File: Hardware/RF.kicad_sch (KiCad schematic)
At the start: 5 parts, among them J2 Conn_Coaxial

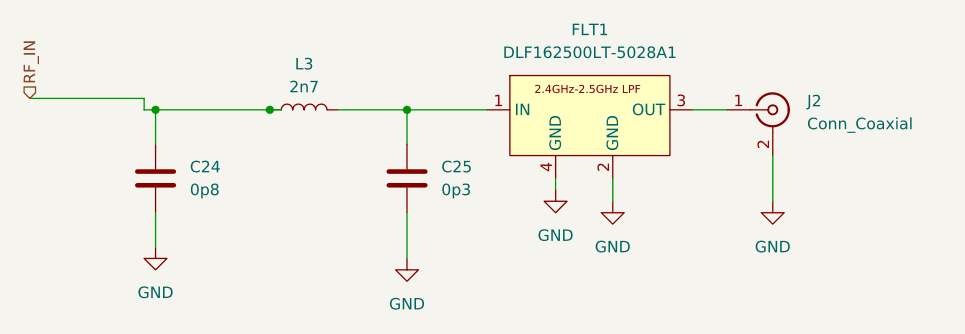
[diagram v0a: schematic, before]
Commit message: [EXECUTION ERC] : Le check électrique a bien marché sauf une erreur persistante sur VLXSMPS ce qui est un défaut du symbole créé et non du montage de découplage proposé par ST Microelectronics
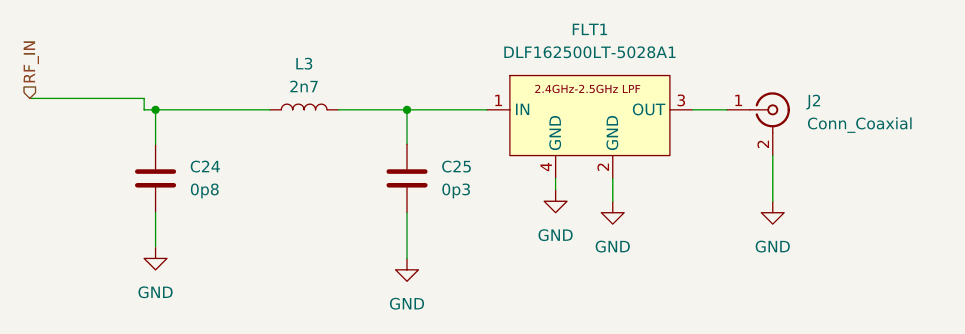
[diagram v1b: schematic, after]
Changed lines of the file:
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@@
 	(paper "A4")
 	(junction
-		(at 107.95 68.58)
+		(at 123.19 68.58)
 		(diameter 0)
 		(color 0 0 0 0)
@@
 		(color 0 0 0 0)
 	)
-	(junction
-		(at 123.19 68.58)
-		(diameter 0)
-		(color 0 0 0 0)
+	(wire
+		(pts
+			(xy 95.25 68.58) (xy 107.95 68.58)
+		)
+		(stroke
+			(width 0)
+			(type default)
+		)
 	)
 	(wire
@@
 	(wire
 		(pts
-			(xy 107.95 68.58) (xy 109.22 68.58)
-		)
-		(stroke
-			(width 0)
-			(type default)
-		)
-	)
-	(wire
-		(pts
 			(xy 115.57 68.58) (xy 123.19 68.58)
 		)
@@
 		(pts
 			(xy 146.05 76.2) (xy 146.05 78.74)
-		)
-		(stroke
-			(width 0)
-			(type default)
-		)
-	)
-	(wire
-		(pts
-			(xy 95.25 68.58) (xy 107.95 68.58)
 		)
 		(stroke
@@
 		(dnp no)
 		(fields_autoplaced yes)
-		(property "Reference" "#PWR?"
+		(property "Reference" "#PWR023"
 			(at 95.25 90.17 0)
 			(effects
@@
 			(project "Hardware"
 				(path "/ba4846b8-7c71-441f-b11b-b34cbea60d05/f30678ac-07b1-44be-9fb4-b413baff1170"
-					(reference "#PWR?")
+					(reference "#PWR023")
 					(unit 1)
 				)
@@
 		(dnp no)
 		(fields_autoplaced yes)
-		(property "Reference" "#PWR?"
+		(property "Reference" "#PWR020"
 			(at 139.7 83.82 0)
 			(effects
@@
 			(project "Hardware"
 				(path "/ba4846b8-7c71-441f-b11b-b34cbea60d05/f30678ac-07b1-44be-9fb4-b413baff1170"
-					(reference "#PWR?")
+					(reference "#PWR020")
 					(unit 1)
 				)
@@
 		(dnp no)
 		(fields_autoplaced yes)
-		(property "Reference" "#PWR?"
+		(property "Reference" "#PWR024"
 			(at 123.19 91.44 0)
 			(effects
@@
 			(project "Hardware"
 				(path "/ba4846b8-7c71-441f-b11b-b34cbea60d05/f30678ac-07b1-44be-9fb4-b413baff1170"
-					(reference "#PWR?")
+					(reference "#PWR024")
 					(unit 1)
 				)
@@
 		(dnp no)
 		(fields_autoplaced yes)
-		(property "Reference" "#PWR?"
+		(property "Reference" "#PWR022"
 			(at 163.83 85.09 0)
 			(effects
@@
 			(project "Hardware"
 				(path "/ba4846b8-7c71-441f-b11b-b34cbea60d05/f30678ac-07b1-44be-9fb4-b413baff1170"
-					(reference "#PWR?")
+					(reference "#PWR022")
 					(unit 1)
 				)
@@
 		(dnp no)
 		(fields_autoplaced yes)
-		(property "Reference" "#PWR?"
+		(property "Reference" "#PWR021"
 			(at 146.05 85.09 0)
 			(effects
@@
 			(project "Hardware"
 				(path "/ba4846b8-7c71-441f-b11b-b34cbea60d05/f30678ac-07b1-44be-9fb4-b413baff1170"
-					(reference "#PWR?")
-					(unit 1)
-				)
+					(reference "#PWR021")
+					(unit 1)
+				)

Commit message: [FOOTPRINT ASSIGNMENT] : Ajout des footprints à chaque élément
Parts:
- C24, C25: footprint (none) -> Capacitor_SMD:C_0402_1005Metric
- J2: footprint (none) -> Connector_Coaxial:U.FL_Hirose_U.FL-R-SMT-1_Vertical
- L3: footprint (none) -> Inductor_SMD:L_0402_1005Metric
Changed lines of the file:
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@@
 			)
 		)
-		(property "Footprint" ""
+		(property "Footprint" "Inductor_SMD:L_0402_1005Metric"
 			(at 111.76 68.58 0)
 			(effects
@@
 			)
 		)
-		(property "Footprint" ""
+		(property "Footprint" "Capacitor_SMD:C_0402_1005Metric"
 			(at 124.1552 80.01 0)
 			(effects
@@
 			)
 		)
-		(property "Footprint" ""
+		(property "Footprint" "Capacitor_SMD:C_0402_1005Metric"
 			(at 96.2152 80.01 0)
 			(effects
@@
 			)
 		)
-		(property "Footprint" ""
+		(property "Footprint" "Connector_Coaxial:U.FL_Hirose_U.FL-R-SMT-1_Vertical"
 			(at 163.83 68.58 0)
 			(effects

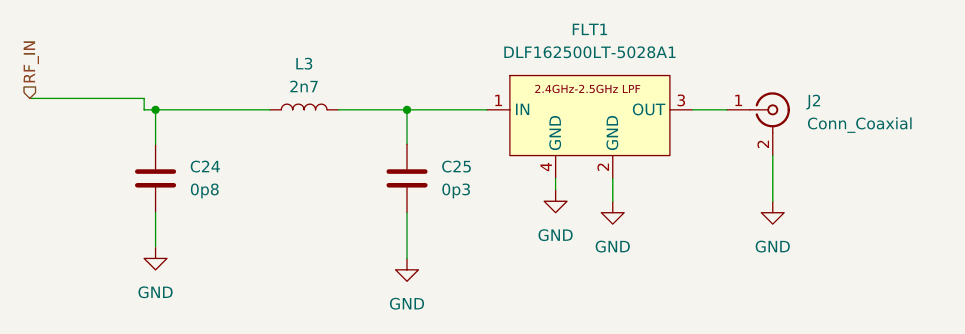
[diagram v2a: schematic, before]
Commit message: [FOOTPRINT ASSIGNMENT] : J'ai ajouté le +5V flag de l'USB, j'ai ajouté des labels pour avoir un netclass plus consistent
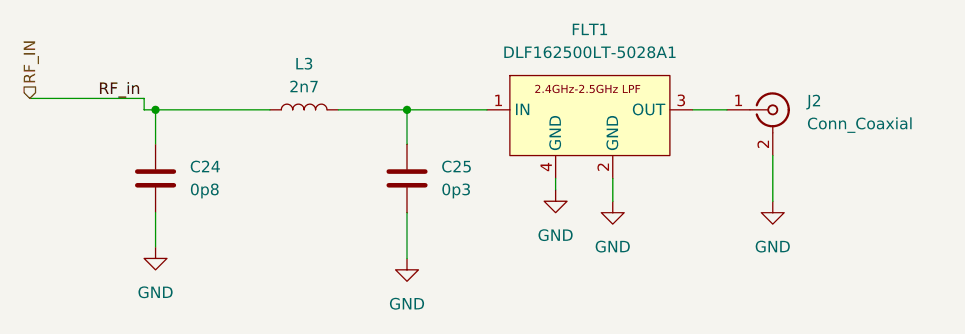
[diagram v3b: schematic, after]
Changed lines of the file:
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@@
+		)
+	)
+	(label "RF_in"
+		(at 88.9 67.31 0)
+		(effects
+			(font
+				(size 1.27 1.27)
+			)
+			(justify left bottom)
 		)
 	)

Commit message: [PLACEMENT DES COMPOSANT ET DIMENSIONNEMENT] : Avant de désigner le type de signal à chaque couche et commencer le routage, j'ai d'abord commencer par organiser les composants selon la schématique et comment j'aimerais avoir le produit finale
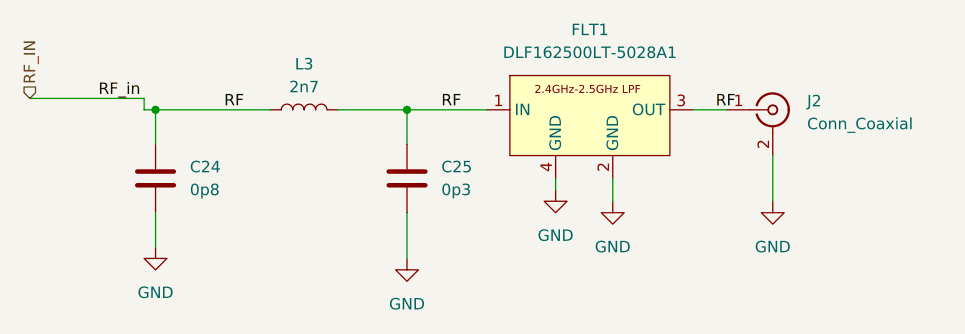
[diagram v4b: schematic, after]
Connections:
- net RF_IN: now also C25.1, FLT1.1 (IN), FLT1.3 (OUT), J2.1 (In), L3.2
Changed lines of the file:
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@@
+		)
+	)
+	(label "RF"
+		(at 102.87 68.58 0)
+		(effects
+			(font
+				(size 1.27 1.27)
+			)
+			(justify left bottom)
+		)
+	)
+	(label "RF"
+		(at 127 68.58 0)
+		(effects
+			(font
+				(size 1.27 1.27)
+			)
+			(justify left bottom)
 		)
 	)
@@
 		(effects
 			(font
+				(size 1.27 1.27)
+			)
+			(justify left bottom)
+		)
+	)
+	(label "RF"
+		(at 157.48 68.58 0)
+		(effects
+			(font

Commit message: [ROUTAGE ET CONTROL DRC] : J'ai routé la carte sur 4 couches. F.cu layer : c'est la prémière couche In1.cu layer: c'est le plan de masse In2.cu layer : c'est le plan de tension 3.3V B.cu layer : c'est pour les signaux qui passent par des via.
J'ai routé le PCB ensuite,j'ai effectué le Test DRC, puis j'ai corrigé
les bug manifeste.
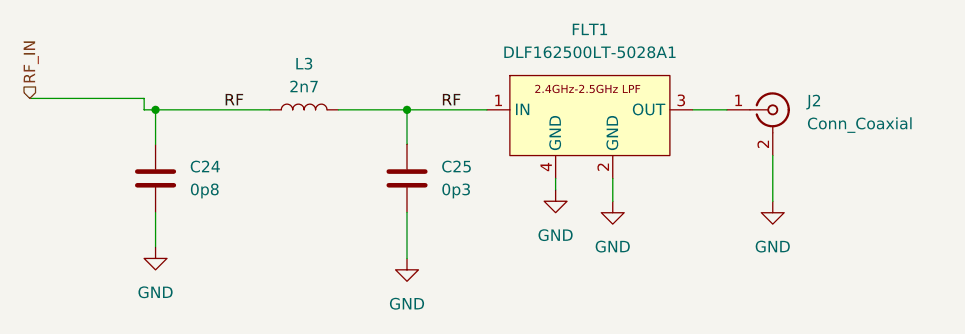
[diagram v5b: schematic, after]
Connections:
- net RF_IN: no longer FLT1.3 (OUT), J2.1 (In)
- new net: FLT1.3 (OUT), J2.1 (In)
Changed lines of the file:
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@@
-		)
-	)
-	(label "RF_in"
-		(at 88.9 67.31 0)
-		(effects
-			(font
-				(size 1.27 1.27)
-			)
-			(justify left bottom)
-		)
-	)
-	(label "RF"
-		(at 157.48 68.58 0)
-		(effects
-			(font
-				(size 1.27 1.27)
-			)
-			(justify left bottom)
 		)
 	)

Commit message: [Bill of Materials(BOM)]: Remplissage des informations tels que : manufacturer part number, manufacturer et la documentation du composant concerné. le BOM sera envoyé avec le fichier Geber au fabricant de PCB
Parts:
- C24: Manufacturer (none) -> Vishay / Vitramon; Manufacturer Part Number (none) -> VJ0402D0R8VXBAJHT
- C25: Manufacturer (none) -> Murata Electronics; Manufacturer Part Number (none) -> GRM1555C1HR30WA01D
- FLT1: Manufacturer (none) -> TDK; Manufacturer Part Number (none) -> DLF162500LT-5028A1
- J2: Manufacturer (none) -> Hirose Connector; Manufacturer Part Number (none) -> U.FL-R-SMT(01)
- L3: Manufacturer (none) -> Murata Electronics; Manufacturer Part Number (none) -> LQG15HS2N7S02D
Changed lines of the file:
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@@
 			)
 		)
-		(property "Datasheet" ""
+		(property "Datasheet" "https://product.tdk.com/system/files/dam/doc/product/rf/rf/filter/catalog/rf_lpf_dlf162500lt-5028a1_en.pdf"
 			(at 143.51 73.66 0)
 			(effects
@@
 			)
 		)
-		(property "Description" ""
+		(property "Description" "Multilayer Low Pass Filter For 2400-2500MHz"
+			(at 143.51 73.66 0)
+			(effects
+				(font
+					(size 1.27 1.27)
+				)
+				(hide yes)
+			)
+		)
+		(property "Manufacturer" "TDK"
+			(at 143.51 73.66 0)
+			(effects
+				(font
+					(size 1.27 1.27)
+				)
+				(hide yes)
+			)
+		)
+		(property "Manufacturer Part Number" "DLF162500LT-5028A1"
 			(at 143.51 73.66 0)
 			(effects
@@
 			)
 		)
-		(property "Datasheet" "~"
+		(property "Datasheet" "https://www.mouser.fr/datasheet/3/76/2/JELF243B_0010.pdf"
 			(at 111.76 68.58 0)
 			(effects
@@
 			)
 		)
+		(property "Manufacturer" "Murata Electronics"
+			(at 111.76 68.58 90)
+			(effects
+				(font
+					(size 1.27 1.27)
+				)
+				(hide yes)
+			)
+		)
+		(property "Manufacturer Part Number" "LQG15HS2N7S02D"
+			(at 111.76 68.58 90)
+			(effects
+				(font
+					(size 1.27 1.27)
+				)
+				(hide yes)
+			)
+		)
 		(pin "2"
 		)
@@
 			)
 		)
-		(property "Datasheet" "~"
+		(property "Datasheet" "https://pim.murata.com/asset/pim4/ceramicCapacitorSMD/GRM1555C1HR30WA01-01A-EN_PDF_CERAMICCAPACITORSMD"
 			(at 123.19 76.2 0)
 			(effects
@@
 			)
 		)
+		(property "Manufacturer" "Murata Electronics"
+			(at 123.19 76.2 0)
+			(effects
+				(font
+					(size 1.27 1.27)
+				)
+				(hide yes)
+			)
+		)
+		(property "Manufacturer Part Number" "GRM1555C1HR30WA01D"
+			(at 123.19 76.2 0)
+			(effects
+				(font
+					(size 1.27 1.27)
+				)
+				(hide yes)
+			)
+		)
 		(pin "1"
 		)
@@
 			)
 		)
-		(property "Datasheet" "~"
+		(property "Datasheet" "https://www.vishay.com/docs/45239/vjhifreqht.pdf"
 			(at 95.25 76.2 0)
 			(effects
@@
 			)
 		)
+		(property "Manufacturer" "Vishay / Vitramon"
+			(at 95.25 76.2 0)
+			(effects
+				(font
+					(size 1.27 1.27)
+				)
+				(hide yes)
+			)
+		)
+		(property "Manufacturer Part Number" "VJ0402D0R8VXBAJHT"
+			(at 95.25 76.2 0)
+			(effects
+				(font
+					(size 1.27 1.27)
+				)
+				(hide yes)
+			)
+		)
 		(pin "2"
 		)
@@
 			)
 		)
-		(property "Datasheet" "~"
+		(property "Datasheet" "https://www.mouser.com/catalog/specsheets/hiros04491-1.pdf"
 			(at 163.83 68.58 0)
 			(effects
@@
 			(at 163.83 68.58 0)
 			(effects
+				(font
+					(size 1.27 1.27)
+				)
+				(hide yes)
+			)
+		)
+		(property "Manufacturer" "Hirose Connector"
+			(at 163.83 68.58 0)
+			(effects
+				(font
+					(size 1.27 1.27)
+				)
+				(hide yes)
+			)
+		)
+		(property "Manufacturer Part Number" "U.FL-R-SMT(01)"
+			(at 163.83 68.58 0)
+			(effects

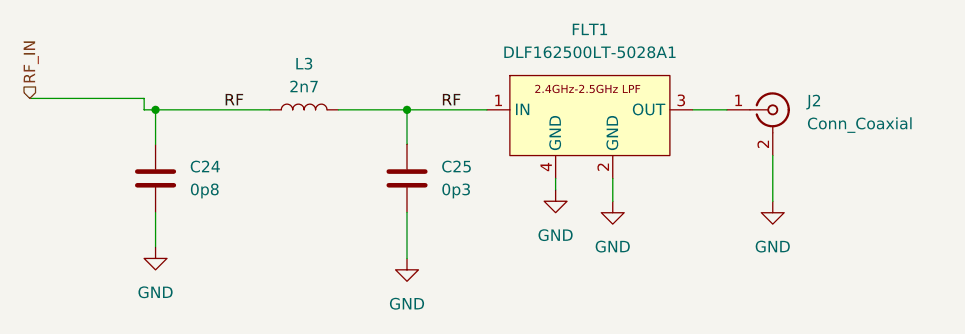
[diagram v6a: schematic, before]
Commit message: [CORRECCTION DU PCB] : J'ai corrigé le PCB après avoir discuter avec le Fabricant PCB Way, j'ai corrigé le footprint de la capacité C14 avec ce qui correspond à ce qui est vendu par mouser electronics. Le bon footprint est 0402_1005. J'ai également corrigé le footprint des connecteurs 01x04 avec un footprint de 2.54mm. Avant c'était 1mm, du coup j'ai modifié le PCB. J'ai également modifier le placement des capacité et des inductances, plus proche du stm32.
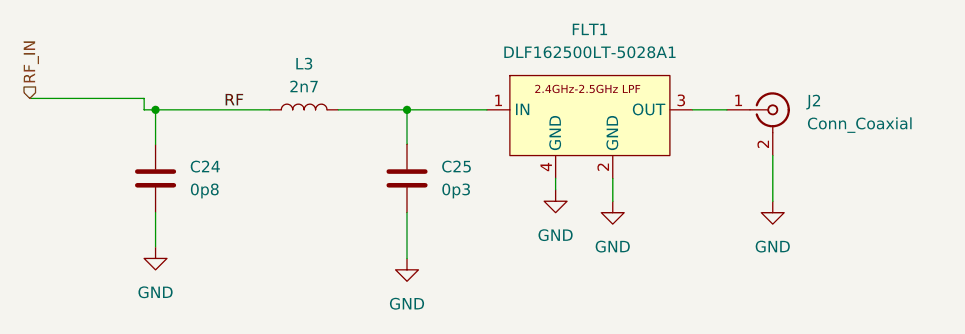
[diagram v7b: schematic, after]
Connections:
- net RF_IN: no longer C25.1, FLT1.1 (IN), L3.2
- new net: C25.1, FLT1.1 (IN), L3.2
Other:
- company: (none) -> PAR KAMDA JONATAN
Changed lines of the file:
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@@
 	(generator_version "9.0")
 	(paper "A4")
+	(title_block
+		(company "PAR KAMDA JONATAN")
+	)
 	(junction
 		(at 123.19 68.58)
@@
 		(effects
 			(font
-				(size 1.27 1.27)
-			)
-			(justify left bottom)
-		)
-	)
-	(label "RF"
-		(at 127 68.58 0)
-		(effects
-			(font
